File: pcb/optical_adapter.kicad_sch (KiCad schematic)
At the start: 24 parts, among them J1 Conn_01x06_Pin, Q1 BC847, Q2 BC847, Q3 BC857, Q5 IRLML2060, U1 LM1117MP-3.3

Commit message: Add part numbers to BOM
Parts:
- C1, C2: MFRNO (none) -> TR3A106K010C1000; MOUSERNO (none) -> 74-TR3A106K010C1000
- D1: MFRNO (none) -> APTR3216P3BT; MOUSERNO (none) -> 604-APTR3216P3BT
- D2: MFRNO (none) -> APTR3216F3C; MOUSERNO (none) -> 604-APTR3216F3C
- D3: MFRNO (none) -> 150120AS75000; MOUSERNO (none) -> 710-150120AS75000
- D4: MFRNO (none) -> 150120GS75000; MOUSERNO (none) -> 710-150120GS75000
- J1: MFRNO (none) -> 68001-406HLF; MOUSERNO (none) -> 649-68001-406HLF
- Q1, Q2: MFRNO (none) -> BC847CLT1G; MOUSERNO (none) -> 863-BC847CLT1G
- Q3: MFRNO (none) -> BC857CLT1G; MOUSERNO (none) -> 863-BC857CLT1G
- Q5: MFRNO (none) -> IRLML2060TRPBF; MOUSERNO (none) -> 942-IRLML2060TRPBF
- R1: MFRNO (none) -> CRCW1206100RJNEA; MOUSERNO (none) -> 71-CRCW1206J-100-E3
- R10, R11: MFRNO (none) -> CRCW12060000ZSTC; MOUSERNO (none) -> 71-CRCW12060000ZSTC
- R2: MFRNO (none) -> CRCW120615K0JNEA; MOUSERNO (none) -> 71-CRCW1206J-15K-E3
- R3: MFRNO (none) -> CRCW120639K0JNEA; MOUSERNO (none) -> 71-CRCW1206J-39K-E3
- R4, R5, R6: MFRNO (none) -> CRCW120610K0JNEA; MOUSERNO (none) -> 71-CRCW1206J-10K-E3
- R7: MFRNO (none) -> CRCW1206220RJNEA; MOUSERNO (none) -> 71-CRCW1206J-220-E3
- R8: MFRNO (none) -> CRCW120691R0JNEA; MOUSERNO (none) -> 71-CRCW1206J-91-E3
- R9: MFRNO (none) -> CRCW12065R60JNEA; MOUSERNO (none) -> 71-CRCW1206J-5.6-E3
- U1: MFRNO (none) -> LM1117MP-3.3/NOPB; MOUSERNO (none) -> 926-LM1117MP-3.3NOPB

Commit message: Add solder bridge between TX and RX circuit
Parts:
- added JP1: SolderJumper_2_Bridged, Jumper:SolderJumper-2_P1.3mm_Open_TrianglePad1.0x1.5mm, symbol Jumper:SolderJumper_2_Bridged
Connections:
- net TX: now also JP1.1 (A); no longer D1.2 (A), Q1.1 (B), R2.1
- new net: D1.2 (A), JP1.2 (B), Q1.1 (B), R2.1
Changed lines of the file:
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@@
+	(wire
+		(pts
+			(xy 63.5 96.52) (xy 66.04 96.52)
+		)
+		(stroke
+			(width 0)
+			(type default)
+		)
+	)
 	(wire
 		(pts
@@
 	(wire
 		(pts
-			(xy 91.44 73.66) (xy 80.01 73.66)
+			(xy 54.61 96.52) (xy 55.88 96.52)
 		)
 		(stroke
@@
 	(wire
 		(pts
-			(xy 43.18 46.99) (xy 49.53 46.99)
+			(xy 91.44 73.66) (xy 80.01 73.66)
 		)
 		(stroke
@@
 	(wire
 		(pts
-			(xy 54.61 96.52) (xy 66.04 96.52)
+			(xy 43.18 46.99) (xy 49.53 46.99)
 		)
 		(stroke
@@
 					(unit 1)
 				)
+			)
+		)
+	)
+	(symbol
+		(lib_id "Jumper:SolderJumper_2_Bridged")
+		(at 59.69 96.52 0)
+		(unit 1)
+		(exclude_from_sim no)
+		(in_bom no)
+		(on_board yes)
+		(dnp no)
+		(fields_autoplaced yes)
+		(property "Reference" "JP1"
+			(at 59.69 90.17 0)
+			(effects
+				(font
+					(size 1.27 1.27)
+				)
+			)
+		)
+		(property "Value" "SolderJumper_2_Bridged"
+			(at 59.69 92.71 0)
+			(effects
+				(font
+					(size 1.27 1.27)
+				)
+				(hide yes)
+			)
+		)
+		(property "Footprint" "Jumper:SolderJumper-2_P1.3mm_Open_TrianglePad1.0x1.5mm"
+			(at 59.69 96.52 0)
+			(effects
+				(font
+					(size 1.27 1.27)
+				)
+				(hide yes)
+			)
+		)
+		(property "Datasheet" "~"
+			(at 59.69 96.52 0)
+			(effects
+				(font
+					(size 1.27 1.27)
+				)
+				(hide yes)
+			)
+		)
+		(property "Description" "Solder Jumper, 2-pole, closed/bridged"
+			(at 59.69 96.52 0)
+			(effects
+				(font
+					(size 1.27 1.27)
+				)
+				(hide yes)
+			)
+		)
+		(property "LCSC" ""
+			(at 59.69 96.52 0)
+			(effects
+				(font
+					(size 1.27 1.27)
+				)
+				(hide yes)
+			)
+		)
+		(pin "2"
+		)
+		(pin "1"
+		)
+		(instances
+			(project ""
+				(path "/eed9174b-005f-42ed-94b9-b0e600055621"
+					(reference "JP1")
+					(unit 1)
+				)

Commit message: Fix the coil active LED
Changed to 150 Ohm to better suite the amber LED and fix incorrect
rotation.
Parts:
- R7: MOUSERNO 71-CRCW1206J-220-E3 -> 71-CRCW1206J-220-E3
- R8: value 91 -> 150; MFRNO CRCW120691R0JNEA -> CRCW1206150RJNEA; MOUSERNO 71-CRCW1206J-91-E3 -> 71-CRCW1206J-150-E3
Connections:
- net +5V: now also D3.2 (A); no longer D3.1 (K)
- net at R8.1: now also D3.1 (K); no longer D3.2 (A)
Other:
- note added: "~18 Ohm"
- moved on the sheet: D3
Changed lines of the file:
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@@
 		(rev "1")
+	)
+	(text "~18 Ohm"
+		(exclude_from_sim no)
+		(at 143.256 42.164 0)
+		(effects
+			(font
+				(size 1.27 1.27)
+			)
+		)
 	)
 	(junction
@@
 			)
 		)
-		(property "MOUSERNO" "71-CRCW1206J-220-E3 "
+		(property "MOUSERNO" "71-CRCW1206J-220-E3"
 			(at 113.03 63.5 90)
 			(effects
@@
 			)
 		)
-		(property "Value" "91"
+		(property "Value" "150"
 			(at 129.54 50.7999 0)
 			(effects
@@
 			)
 		)
-		(property "MFRNO" "CRCW120691R0JNEA"
+		(property "MFRNO" "CRCW1206150RJNEA"
 			(at 127 49.53 0)
 			(effects
@@
 			)
 		)
-		(property "MOUSERNO" "71-CRCW1206J-91-E3"
+		(property "MOUSERNO" "71-CRCW1206J-150-E3"
 			(at 127 49.53 0)
 			(effects
@@
 		(lib_id "Device:LED")
 		(at 127 36.83 270)
+		(mirror x)
 		(unit 1)
 		(exclude_from_sim no)
@@
 		(on_board yes)
 		(dnp no)
-		(fields_autoplaced yes)
 		(property "Reference" "D3"
-			(at 129.54 33.9724 90)
+			(at 129.54 39.6876 90)
 			(effects
 				(font
@@
 		)
 		(property "Value" "LED"
-			(at 129.54 36.5124 90)
-			(effects
-				(font
+			(at 129.54 37.1476 90)
+			(effects
+				(font

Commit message: Update symbols
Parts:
- L1: footprint footprints:26_turn_16_dia_5_mil -> PCB Coils:4l_26_turn_16_dia_5_mil
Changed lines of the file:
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@@
 			)
 		)
-		(property "Footprint" "footprints:26_turn_16_dia_5_mil"
+		(property "Footprint" "PCB Coils:4l_26_turn_16_dia_5_mil"
 			(at 134.62 41.91 0)
 			(effects
@@
 			)
 		)
-		(property "Datasheet" "https://www.mouser.se/datasheet/3/101/1/BC846ALT1-D.PDF"
+		(property "Datasheet" "http://www.infineon.com/dgdl/Infineon-BC847SERIES_BC848SERIES_BC849SERIES_BC850SERIES-DS-v01_01-en.pdf?fileId=db3a304314dca389011541d4630a1657"
 			(at 88.9 107.95 0)
 			(effects
@@
 	)
 	(symbol
+		(lib_name "LED_1")
 		(lib_id "Device:LED")
 		(at 127 36.83 270)
@@
 			)
 		)
-		(property "Datasheet" "https://www.we-online.com/components/products/datasheet/150120AS75000.pdf"
+		(property "Datasheet" "~"
 			(at 127 36.83 0)
 			(effects
@@
 		(property "MOUSERNO" "710-150120AS75000 "
 			(at 127 36.83 90)
+			(effects
+				(font
+					(size 1.27 1.27)
+				)
+				(hide yes)
+			)
+		)
+		(property "Sim.Pins" "1=K 2=A"
+			(at 127 36.83 0)
 			(effects
 				(font
@@
 	)
 	(symbol
+		(lib_name "BC847_1")
 		(lib_id "Transistor_BJT:BC847")
 		(at 77.47 96.52 0)
@@
 			)
 		)
-		(property "Datasheet" "https://www.mouser.se/datasheet/3/101/1/BC846ALT1-D.PDF"
+		(property "Datasheet" "http://www.infineon.com/dgdl/Infineon-BC847SERIES_BC848SERIES_BC849SERIES_BC850SERIES-DS-v01_01-en.pdf?fileId=db3a304314dca389011541d4630a1657"
 			(at 77.47 96.52 0)
 			(effects
@@
 			)
 		)
-		(property "Datasheet" "https://www.mouser.se/datasheet/3/70/1/Infineon_IRLML2060_DataSheet_v01_01_EN.pdf"
+		(property "Datasheet" "https://www.infineon.com/dgdl/irlml2060pbf.pdf?fileId=5546d462533600a401535664b7fb25ee"
 			(at 133.35 67.31 0)
 			(effects
@@
 		(on_board yes)
 		(dnp no)
-		(fields_autoplaced yes)
 		(property "Reference" "JP1"
-			(at 59.69 90.17 0)
+			(at 59.69 94.488 0)
 			(effects
 				(font
@@
 	)
 	(symbol
+		(lib_name "LED_2")
 		(lib_id "Device:LED")
 		(at 40.64 113.03 90)
@@
 			)
 		)
-		(property "Datasheet" "https://www.kingbrightusa.com/images/catalog/SPEC/APTR3216F3C.pdf"
+		(property "Datasheet" "~"
 			(at 40.64 113.03 0)
 			(effects
@@
 		(property "MOUSERNO" "604-APTR3216F3C "
 			(at 40.64 113.03 90)
+			(effects
+				(font
+					(size 1.27 1.27)
+				)
+				(hide yes)
+			)
+		)
+		(property "Sim.Pins" "1=K 2=A"
+			(at 40.64 113.03 0)
 			(effects
 				(font
@@
 			)
 		)
-		(property "Datasheet" "https://www.mouser.se/datasheet/3/101/1/BC856ALT1-D.PDF"
+		(property "Datasheet" "https://www.onsemi.com/pub/Collateral/BC860-D.pdf"
 			(at 43.18 82.55 0)
 			(effects
@@
 			)
 		)
-		(property "Datasheet" "https://www.we-online.com/components/products/datasheet/150120GS75000.pdf"
+		(property "Datasheet" "~"
 			(at 59.69 45.72 0)
 			(effects
@@
 			(effects
 				(font
+					(size 1.27 1.27)
+				)
+				(hide yes)
+			)
+		)
+		(property "Sim.Pins" "1=K 2=A"
+			(at 59.69 45.72 0)
+			(effects
+				(font

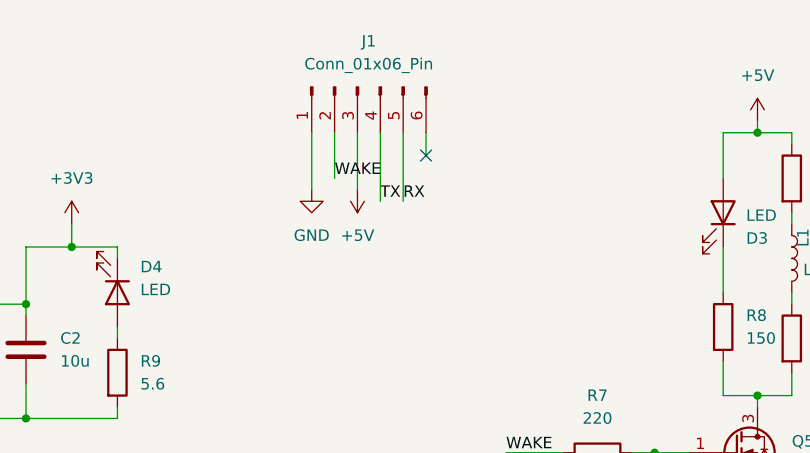
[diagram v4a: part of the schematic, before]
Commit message: Move the coil wake up signal to RTS
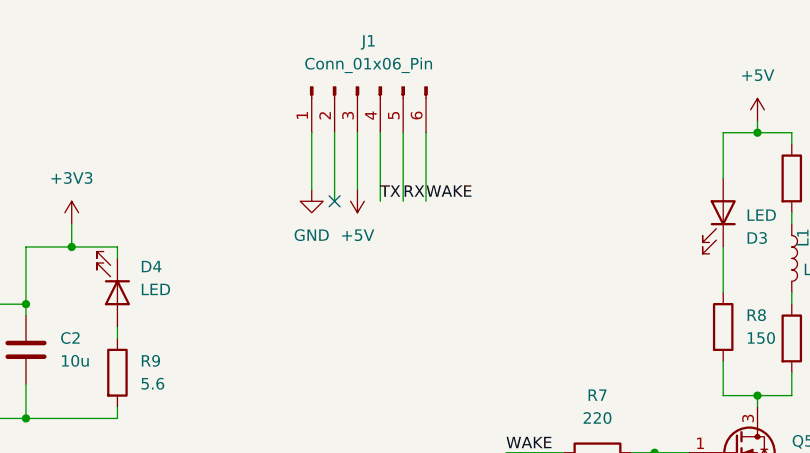
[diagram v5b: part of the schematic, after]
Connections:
- net WAKE: now also J1.6 (Pin_6); no longer J1.2 (Pin_2)
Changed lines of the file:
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@@
 	)
 	(no_connect
-		(at 93.98 30.48)
+		(at 83.82 35.56)
 	)
 	(wire
@@
 	(wire
 		(pts
+			(xy 83.82 27.94) (xy 83.82 35.56)
+		)
+		(stroke
+			(width 0)
+			(type default)
+		)
+	)
+	(wire
+		(pts
 			(xy 125.73 76.2) (xy 130.81 76.2)
 		)
@@
 	(wire
 		(pts
-			(xy 93.98 27.94) (xy 93.98 30.48)
-		)
-		(stroke
-			(width 0)
-			(type default)
-		)
-	)
-	(wire
-		(pts
-			(xy 83.82 27.94) (xy 83.82 33.02)
-		)
-		(stroke
-			(width 0)
-			(type default)
-		)
-	)
-	(wire
-		(pts
 			(xy 40.64 73.66) (xy 66.04 73.66)
 		)
@@
 		(pts
 			(xy 59.69 49.53) (xy 59.69 50.8)
+		)
+		(stroke
+			(width 0)
+			(type default)
+		)
+	)
+	(wire
+		(pts
+			(xy 93.98 35.56) (xy 93.98 27.94)
 		)
 		(stroke
@@
 	)
 	(label "WAKE"
-		(at 83.82 33.02 0)
+		(at 93.98 35.56 0)
 		(effects
 			(font
